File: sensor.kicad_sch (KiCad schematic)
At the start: 144 parts, among them IC1 A3909, J1 Micro_SD_Card_Det1, J12 Conn_01x04, J13 1x3 servo, J14 1x3 servo, J15 arming terminal, J16 arming terminal, J17 arming terminal, J18 arming terminal, J19 Screw_Terminal_01x02, J20 Screw_Terminal_01x02, J21 Screw_Terminal_01x02, J22 Screw_Terminal_01x02, J25 Conn_Coaxial, J3 Conn_Coaxial, J4 H9161TR-ND, J5 Screw_Term, J6 1x3 servo, J9 1x3 servo, Q1 IRLML6402, Q10 IRLML6402, Q11 IRLML6402, Q3 IRLML6402, Q4 IRLML6402, Q5 IRLML6402, Q6 IRLML6402, Q7 BSS138, Q8 IRLML6402, Q9 IRLML6402, U10 LSM6DS3, U11 BGM220SC12WGA2R, U2 IMU, U5 LPS22HB, U6 GPS, U7 SX1276, U8 NAND, Y2 32.768kHz

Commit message: Merged Fix of Schematic and PCB
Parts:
- C4: footprint (none) -> Capacitor_SMD:C_0603_1608Metric
- L3, L7: footprint (none) -> Inductor_SMD:L_6.3x6.3_H3
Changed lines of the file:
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@@
 			)
 		)
-		(property "Footprint" ""
+		(property "Footprint" "Inductor_SMD:L_6.3x6.3_H3"
 			(at 124.46 160.02 0)
 			(effects
@@
 			)
 		)
-		(property "Footprint" ""
+		(property "Footprint" "Inductor_SMD:L_6.3x6.3_H3"
 			(at -24.13 91.44 0)
 			(effects
@@
 			)
 		)
-		(property "Footprint" ""
+		(property "Footprint" "Capacitor_SMD:C_0603_1608Metric"
 			(at -14.2748 91.44 0)
 			(effects

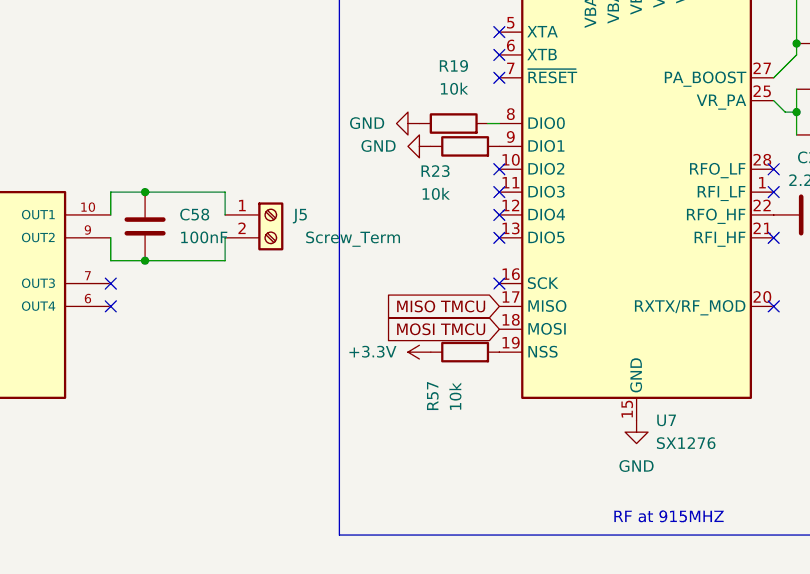
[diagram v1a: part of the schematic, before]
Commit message: CS, and SCK for RF
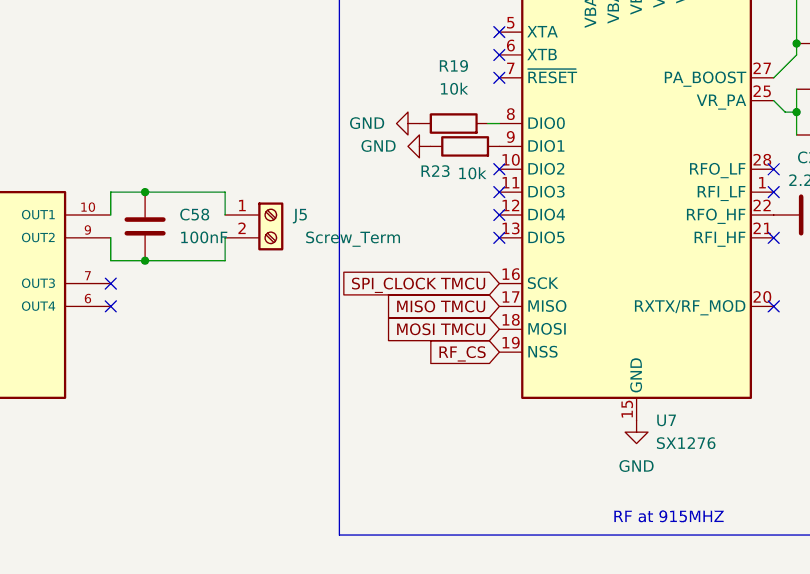
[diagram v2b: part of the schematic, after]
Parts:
- removed R57: 10k, Resistor_SMD:R_0603_1608Metric, symbol Device:R
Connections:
- net SPI_CLOCK TMCU: now also U7.16 (SCK)
- net RF_CS: now reaches U7.19 (NSS)
- no-connect marks 55 -> 54
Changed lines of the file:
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@@
 	)
 	(no_connect
-		(at 76.2 167.64)
-	)
-	(no_connect
 		(at 227.33 151.13)
 	)
@@
 		)
 	)
+	(global_label "SPI_CLOCK TMCU"
+		(shape input)
+		(at 76.2 167.64 180)
+		(fields_autoplaced yes)
+		(effects
+			(font
+				(size 1.27 1.27)
+			)
+			(justify right)
+		)
+		(property "Intersheetrefs" "${INTERSHEET_REFS}"
+			(at 57.0072 167.64 0)
+			(effects
+				(font
+					(size 1.27 1.27)
+				)
+				(justify right)
+				(hide yes)
+			)
+		)
+	)
 	(global_label "MISO TMCU"
 		(shape input)
@@
 		)
 	)
+	(global_label "RF_CS"
+		(shape input)
+		(at 76.2 175.26 180)
+		(fields_autoplaced yes)
+		(effects
+			(font
+				(size 1.27 1.27)
+			)
+			(justify right)
+		)
+		(property "Intersheetrefs" "${INTERSHEET_REFS}"
+			(at 67.4091 175.26 0)
+			(effects
+				(font
+					(size 1.27 1.27)
+				)
+				(justify right)
+				(hide yes)
+			)
+		)
+	)
 	(global_label "SERVO2"
 		(shape input)
@@
 	)
 	(symbol
-		(lib_id "Device:R")
-		(at 72.39 175.26 90)
-		(unit 1)
-		(exclude_from_sim no)
-		(in_bom yes)
-		(on_board yes)
-		(dnp no)
-		(property "Reference" "R57"
-			(at 68.834 181.864 0)
-			(effects
-				(font
-					(size 1.27 1.27)
-				)
-				(justify left)
-			)
-		)
-		(property "Value" "10k"
-			(at 71.374 181.864 0)
-			(effects
-				(font
-					(size 1.27 1.27)
-				)
-				(justify left)
-			)
-		)
-		(property "Footprint" "Resistor_SMD:R_0603_1608Metric"
-			(at 72.39 177.038 90)
-			(effects
-				(font
-					(size 1.27 1.27)
-				)
-				(hide yes)
-			)
-		)
-		(property "Datasheet" "~"
-			(at 72.39 175.26 0)
-			(effects
-				(font
-					(size 1.27 1.27)
-				)
-				(hide yes)
-			)
-		)
-		(property "Description" "Resistor"
-			(at 72.39 175.26 0)
-			(effects
-				(font
-					(size 1.27 1.27)
-				)
-				(hide yes)
-			)
-		)
-		(pin "1"
-		)
-		(pin "2"
-		)
-		(instances
-			(project "horizon"
-				(path "/78d9c2f3-deae-418a-8c21-4820ea8fc57f/8017925a-458a-4a0a-8733-ba805a96612a"
-					(reference "R57")
-					(unit 1)
-				)
-			)
-		)
-	)
-	(symbol
 		(lib_id "power:GND")
 		(at 93.98 72.39 90)
@@
 		)
 		(property "Value" "10k"
-			(at 69.088 157.734 90)
+			(at 73.152 155.448 90)
 			(effects
 				(font
@@
 					(unit 1)
 				)
-			)
-		)
-	)
-	(symbol
-		(lib_id "power:+3.3V")
-		(at 68.58 175.26 90)
-		(unit 1)
-		(exclude_from_sim no)
-		(in_bom yes)
-		(on_board yes)
-		(dnp no)
-		(fields_autoplaced yes)
-		(property "Reference" "#PWR0155"
-			(at 72.39 175.26 0)
-			(effects
-				(font
-					(size 1.27 1.27)
-				)
-				(hide yes)
-			)
-		)
-		(property "Value" "+3.3V"
-			(at 64.77 175.2599 90)
-			(effects
-				(font
-					(size 1.27 1.27)
-				)
-				(justify left)
-			)
-		)
-		(property "Footprint" ""
-			(at 68.58 175.26 0)
-			(effects
-				(font
-					(size 1.27 1.27)
-				)
-				(hide yes)
-			)
-		)
-		(property "Datasheet" ""
-			(at 68.58 175.26 0)
-			(effects
-				(font
-					(size 1.27 1.27)
-				)
-				(hide yes)
-			)
-		)
-		(property "Description" "Power symbol creates a global label with name \"+3.3V\""
-			(at 68.58 175.26 0)
-			(effects
-				(font
-					(size 1.27 1.27)
-				)
-				(hide yes)
-			)
-		)
-		(pin "1"
-		)
-		(instances
-			(project "horizon"
-				(path "/78d9c2f3-deae-418a-8c21-4820ea8fc57f/8017925a-458a-4a0a-8733-ba805a96612a"
-					(reference "#PWR0155")
-					(unit 1)
-				)

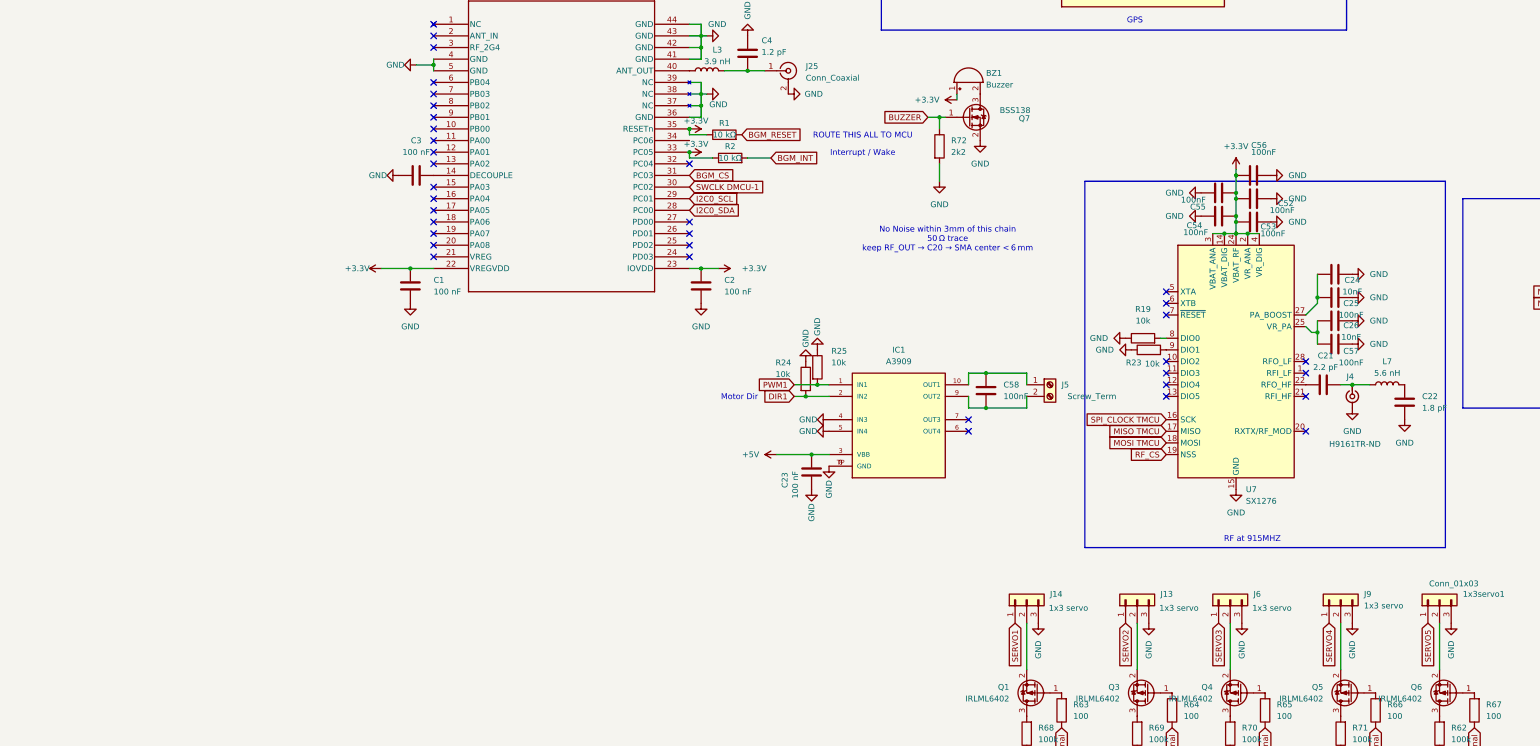
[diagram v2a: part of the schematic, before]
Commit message: do some rf routing (and hopefully not break everything)
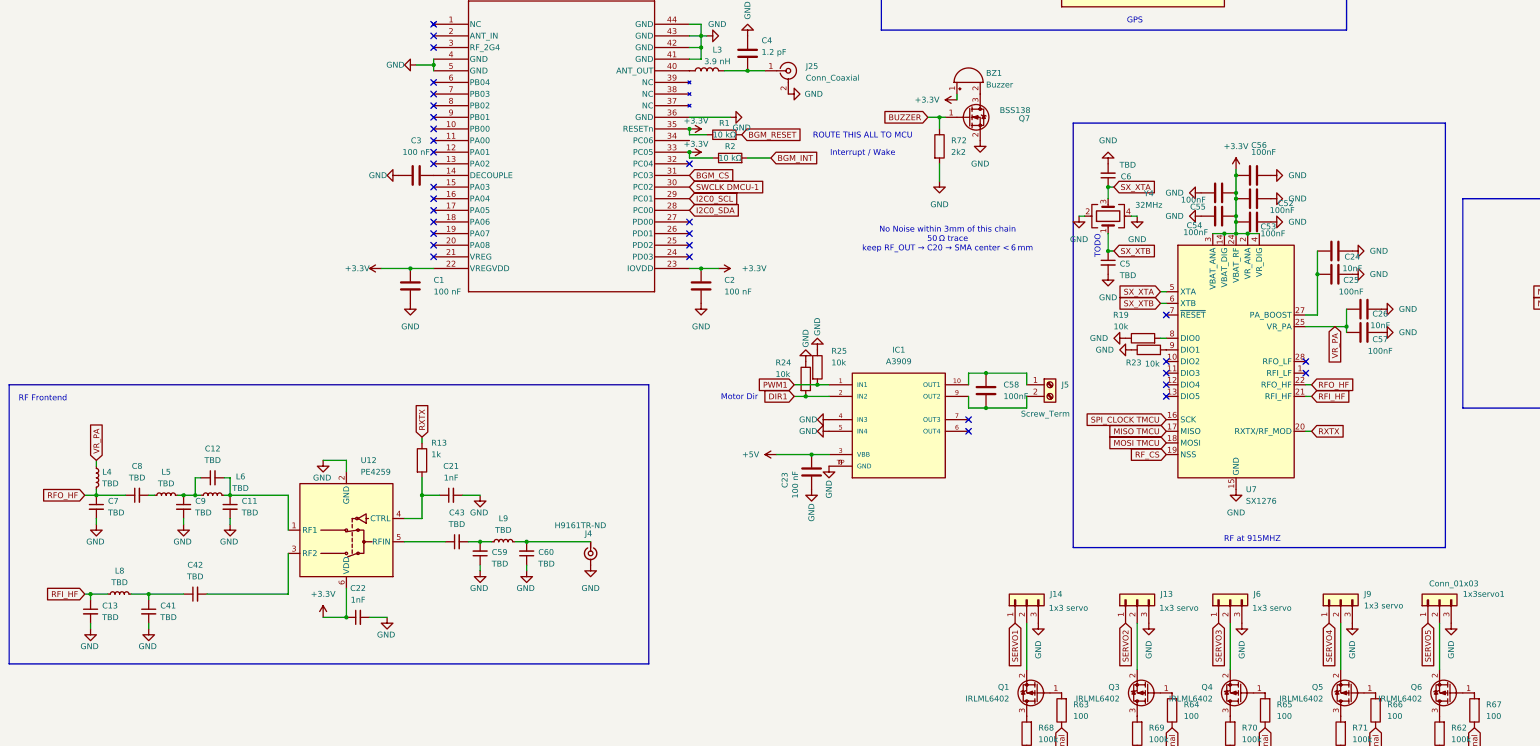
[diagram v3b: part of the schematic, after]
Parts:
- removed C21: 2.2 pF, Capacitor_SMD:C_0603_1608Metric, symbol Device:C
- removed C22: 1.8 pF, Capacitor_SMD:C_0603_1608Metric, symbol Device:C
- removed L7: 5.6 nH, Inductor_SMD:L_6.3x6.3_H3, symbol Device:L
- added C11, C12, C13, C41, C42, C43, C5, C59, C6, C60, C7, C8, C9: TBD, Capacitor_SMD:C_0603_1608Metric, symbol Device:C_Small
- added C21, C22: 1nF, Capacitor_SMD:C_0603_1608Metric, symbol Device:C_Small
- added L4, L5, L6, L8, L9: TBD, Inductor_SMD:L_0603_1608Metric, symbol Device:L_Small
- added R13: 1k, Resistor_SMD:R_0603_1608Metric, symbol Device:R
- added U12: PE4259, Package_TO_SOT_SMD:SOT-363_SC-70-6, symbol RF_Switch:BGS12WN6E6327
- added Y4: 32MHz, Crystal:Crystal_SMD_Abracon_ABM10-4Pin_2.5x2.0mm, symbol Device:Crystal_GND24
- J25, J3: footprint SMA:LPRS_SMA_CONNECTOR -> Conn_Coaxial:LPRS_SMA_CONNECTOR
- J4: footprint U.FL:HRS_U.FL-R-SMT_01_ -> H9161TR-ND:HRS_U.FL-R-SMT_01_
- L1, L3: footprint Inductor_SMD:L_6.3x6.3_H3 -> Inductor_SMD:L_0603_1608Metric
- U11: footprint BGM220S_SIL:BGM220SC12WGA2R -> BGM220SC12WGA2R:BGM220SC12WGA2R
- U2: footprint BNO086:IC_BNO086 -> IMU:IC_BNO086
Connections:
- net +3.3V: now also C22.1, U12.6 (VDD)
- net GND: now also C11.2, C13.2, C21.2, C22.2, C41.2, C5.2, C59.1, C6.2, C60.1, C7.2, C9.2, U12.2 (GND), Y4.2, Y4.4; no longer U11.37 (NC), U11.38 (NC), U11.39 (NC)
- net at J4.1 (In): now also C60.2, L9.2
- net VR_PA: now reaches C26.1, C57.1, U7.25 (VR_PA)
- net VR_PA: now also L4.1
- net RXTX: now reaches U7.20 (RXTX/RF_MOD)
- net RXTX: now also R13.1
- net RFI_HF: now reaches U7.21 (RFI_HF)
- net RFI_HF: now also C13.1, L8.1
- net RFO_HF: now reaches U7.22 (RFO_HF)
- net RFO_HF: now also C7.1, C8.1, L4.2
- net SX_XTA: now reaches U7.5 (XTA)
- net SX_XTA: now also C6.1, Y4.3
- net SX_XTB: now reaches U7.6 (XTB)
- net SX_XTB: now also C5.1, Y4.1
- new net: C41.1, C42.1, L8.2
- new net: C43.2, C59.2, L9.1
- new net: C21.1, R13.2, U12.4 (CTRL)
- new net: C8.2, L5.1
- new net: C43.1, U12.5 (RFIN)
- new net: C12.1, C9.1, L5.2, L6.1
- new net: C42.2, U12.3 (RF2)
- new net: C11.1, C12.2, L6.2, U12.1 (RF1)
- no-connect marks 54 -> 50
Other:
- note added: "RF Frontend"
- note added: "TODO"
- moved on the sheet: C24, C25, C26, C57, J4

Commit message: flipped sides, changed footprint
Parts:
- 1x3servo1: footprint Connector_PinSocket_2.54mm:PinSocket_1x03_P2.54mm_Vertical -> Connector_PinHeader_2.54mm:PinHeader_1x03_P2.54mm_Vertical
- J12: footprint Connector_PinSocket_2.54mm:PinSocket_1x04_P2.54mm_Vertical -> Connector_PinHeader_2.54mm:PinHeader_1x04_P2.54mm_Vertical
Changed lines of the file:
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@@
 			)
 		)
-		(property "Footprint" "Connector_PinSocket_2.54mm:PinSocket_1x04_P2.54mm_Vertical"
+		(property "Footprint" "Connector_PinHeader_2.54mm:PinHeader_1x04_P2.54mm_Vertical"
 			(at 189.23 208.28 0)
 			(effects
@@
 			)
 		)
-		(property "Footprint" "Connector_PinSocket_2.54mm:PinSocket_1x03_P2.54mm_Vertical"
+		(property "Footprint" "Connector_PinHeader_2.54mm:PinHeader_1x03_P2.54mm_Vertical"
 			(at 135.89 207.01 0)
 			(effects

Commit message: kinda redid layout
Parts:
- U2: footprint IMU:IC_BNO086 -> BNO086:IC_BNO086
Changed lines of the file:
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@@
 		(at 355.6 41.91)
 	)
-	(bus_entry
-		(at 248.92 107.95)
-		(size 2.54 2.54)
-		(stroke
-			(width 0)
-			(type default)
-		)
-	)
 	(wire
 		(pts
@@
 			)
 		)
-		(property "Footprint" "IMU:IC_BNO086"
+		(property "Footprint" "BNO086:IC_BNO086"
 			(at 232.41 43.18 0)
 			(effects

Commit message: finished layout
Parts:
- J25, J3: footprint Conn_Coaxial:LPRS_SMA_CONNECTOR -> SMA_CONNECTOR:LPRS_SMA_CONNECTOR
- J4: footprint H9161TR-ND:HRS_U.FL-R-SMT_01_ -> KiCADv6:BGM220SC12WGA2R
- U11: footprint BGM220SC12WGA2R:BGM220SC12WGA2R -> KiCADv6:BGM220SC12WGA2R
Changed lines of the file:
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@@
 			)
 		)
-		(property "Footprint" "Conn_Coaxial:LPRS_SMA_CONNECTOR"
+		(property "Footprint" "SMA_CONNECTOR:LPRS_SMA_CONNECTOR"
 			(at -6.35 91.44 0)
 			(effects
@@
 			)
 		)
-		(property "Footprint" "Conn_Coaxial:LPRS_SMA_CONNECTOR"
+		(property "Footprint" "SMA_CONNECTOR:LPRS_SMA_CONNECTOR"
 			(at 113.03 45.72 0)
 			(effects
@@
 			)
 		)
-		(property "Footprint" "BGM220SC12WGA2R:BGM220SC12WGA2R"
+		(property "Footprint" "KiCADv6:BGM220SC12WGA2R"
 			(at -83.82 81.28 0)
 			(effects
@@
 			)
 		)
-		(property "Footprint" "H9161TR-ND:HRS_U.FL-R-SMT_01_"
+		(property "Footprint" "KiCADv6:BGM220SC12WGA2R"
 			(at -49.53 196.85 0)
 			(effects
